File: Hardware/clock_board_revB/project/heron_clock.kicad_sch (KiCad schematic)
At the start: 110 parts, among them J1 5V_IN, J10 PPS_B200_2, J2 PPS_IN, J3 REF_B210_1, J4 REF_B210_2, J5 REF_B200_1, J6 REF_B200_2, J7 PPS_B210_1, J8 PPS_B210_2, J9 PPS_B200_1, U1 TPS7A2033DBVR, U2 TPS7A2033DBVR, U3 SiT5155AI-FK-33E0-10.000000, U4 LMK1C1104PWR, U5 SN74LVC1G17DBVR, U6 SN74LVC125APWR

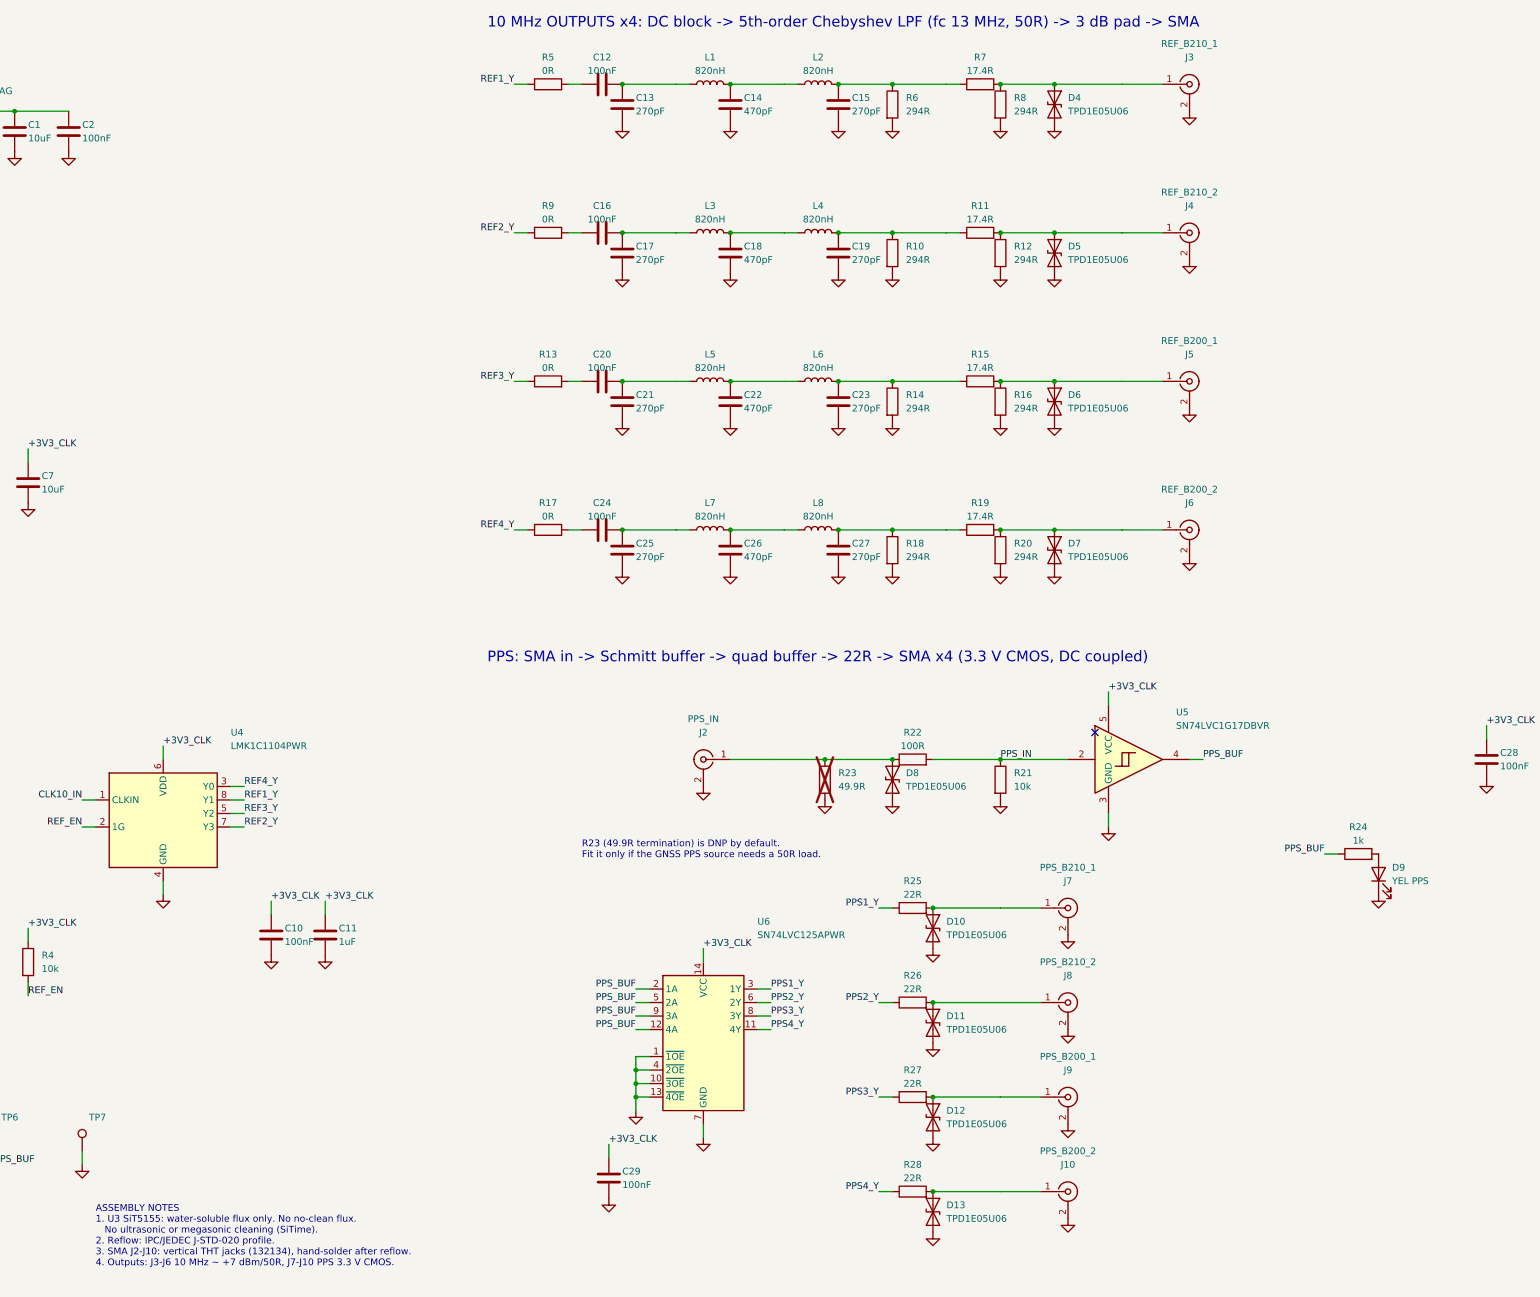
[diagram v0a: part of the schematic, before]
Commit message: Change clock board rev B SDR jacks to SMP blind-mate (D-027)
Change J3-J10 from vertical SMA jacks to Amphenol RF SMP-MSLD-PCT
limited-detent jacks. J2 (PPS IN) stays SMA. The new footprint has
oversize holes (+/-0.20 mm float), so each jack is soldered in place
with its SDR mated. Lead sizes come from the Amphenol IGES model.

Swap the footprints in the existing PCB and keep all routes. Refill
the pours. Move the board title 0.5 mm clear of the larger pads.
Set the R23 DNP flag to match the schematic. Save in KiCad 10 format.
DRC: 0 errors, 0 unconnected pads, 0 parity issues.

Add an export-only mode to make_fab.sh, and let it run on Windows.
Record D-027 and the open values (Q-015) in docs/DECISIONS.md.

Co-Authored-By: Claude Opus 5.5 <noreply@anthropic.com>
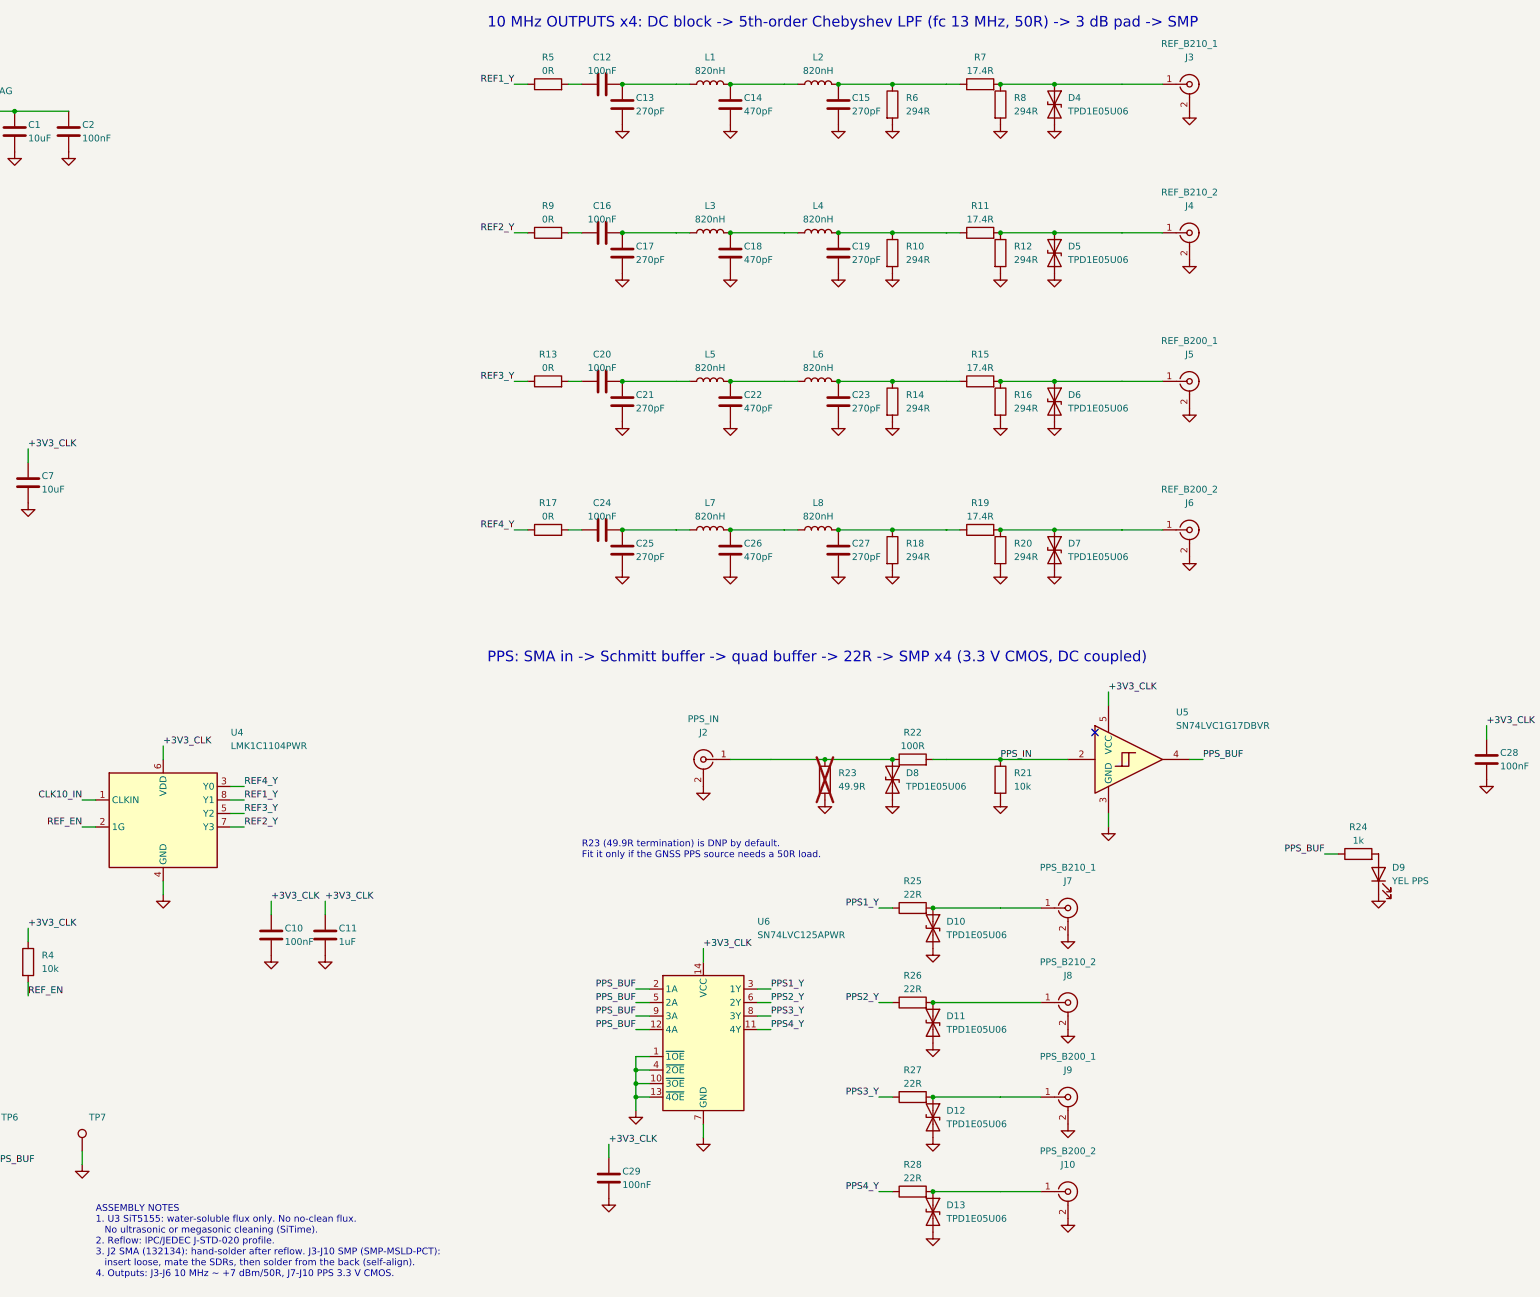
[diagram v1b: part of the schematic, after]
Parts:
- J10, J3, J4, J5, J6, J7, J8, J9: footprint Connector_Coaxial:SMA_Amphenol_132134_Vertical -> HERON_Clock:SMP_Amphenol_SMP-MSLD-PCT_Vertical_Float; MPN 132134 -> SMP-MSLD-PCT
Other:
- note added: "10 MHz OUTPUTS x4: DC block -> 5th-order Chebyshev LPF (fc 13 MHz, 50R) -> 3 dB pad -> SMP"
- note added: "ASSEMBLY NOTES 1. U3 SiT5155: water-soluble flux only. No no-clean flux. No ultrasonic or megasonic cleaning (SiTime). 2. Reflow: IPC/JEDEC J-STD-020 profile. 3. J2 SMA (132134): hand-solder after reflow. J3-J10 SMP (SMP-MSLD-PCT): insert loose, mate the SDRs, then solder from the back (self-align). 4. Outputs: J3-J6 10 MHz ~ +7 dBm/50R, J7-J10 PPS 3.3 V CMOS."
- note added: "PPS: SMA in -> Schmitt buffer -> quad buffer -> 22R -> SMP x4 (3.3 V CMOS, DC coupled)"
- note removed: "10 MHz OUTPUTS x4: DC block -> 5th-order Chebyshev LPF (fc 13 MHz, 50R) -> 3 dB pad -> SMA"
- note removed: "ASSEMBLY NOTES 1. U3 SiT5155: water-soluble flux only. No no-clean flux. No ultrasonic or megasonic cleaning (SiTime). 2. Reflow: IPC/JEDEC J-STD-020 profile. 3. SMA J2-J10: vertical THT jacks (132134), hand-solder after reflow. 4. Outputs: J3-J6 10 MHz ~ +7 dBm/50R, J7-J10 PPS 3.3 V CMOS."
- note removed: "PPS: SMA in -> Schmitt buffer -> quad buffer -> 22R -> SMA x4 (3.3 V CMOS, DC coupled)"
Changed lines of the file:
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@@
           (reference "#PWR020")
           (unit 1)))))
-  (text "10 MHz OUTPUTS x4: DC block -> 5th-order Chebyshev LPF (fc 13 MHz, 50R) -> 3 dB pad -> SMA"
+  (text "10 MHz OUTPUTS x4: DC block -> 5th-order Chebyshev LPF (fc 13 MHz, 50R) -> 3 dB pad -> SMP"
     (at 200.66 22.86 0)
     (effects
@@
         (font
           (size 1.27 1.27))))
-    (property "Footprint" "Connector_Coaxial:SMA_Amphenol_132134_Vertical"
+    (property "Footprint" "HERON_Clock:SMP_Amphenol_SMP-MSLD-PCT_Vertical_Float"
       (at 332.74 35.56 0)
       (effects
@@
         (font
           (size 1.27 1.27)) hide))
-    (property "MPN" "132134"
+    (property "MPN" "SMP-MSLD-PCT"
       (at 332.74 35.56 0)
       (effects
@@
         (font
           (size 1.27 1.27))))
-    (property "Footprint" "Connector_Coaxial:SMA_Amphenol_132134_Vertical"
+    (property "Footprint" "HERON_Clock:SMP_Amphenol_SMP-MSLD-PCT_Vertical_Float"
       (at 332.74 63.5 0)
       (effects
@@
         (font
           (size 1.27 1.27)) hide))
-    (property "MPN" "132134"
+    (property "MPN" "SMP-MSLD-PCT"
       (at 332.74 63.5 0)
       (effects
@@
         (font
           (size 1.27 1.27))))
-    (property "Footprint" "Connector_Coaxial:SMA_Amphenol_132134_Vertical"
+    (property "Footprint" "HERON_Clock:SMP_Amphenol_SMP-MSLD-PCT_Vertical_Float"
       (at 332.74 91.44 0)
       (effects
@@
         (font
           (size 1.27 1.27)) hide))
-    (property "MPN" "132134"
+    (property "MPN" "SMP-MSLD-PCT"
       (at 332.74 91.44 0)
       (effects
@@
         (font
           (size 1.27 1.27))))
-    (property "Footprint" "Connector_Coaxial:SMA_Amphenol_132134_Vertical"
+    (property "Footprint" "HERON_Clock:SMP_Amphenol_SMP-MSLD-PCT_Vertical_Float"
       (at 332.74 119.38 0)
       (effects
@@
         (font
           (size 1.27 1.27)) hide))
-    (property "MPN" "132134"
+    (property "MPN" "SMP-MSLD-PCT"
       (at 332.74 119.38 0)
       (effects
@@
           (reference "#PWR048")
           (unit 1)))))
-  (text "PPS: SMA in -> Schmitt buffer -> quad buffer -> 22R -> SMA x4 (3.3 V CMOS, DC coupled)"
+  (text "PPS: SMA in -> Schmitt buffer -> quad buffer -> 22R -> SMP x4 (3.3 V CMOS, DC coupled)"
     (at 200.66 142.24 0)
     (effects
@@
         (font
           (size 1.27 1.27))))
-    (property "Footprint" "Connector_Coaxial:SMA_Amphenol_132134_Vertical"
+    (property "Footprint" "HERON_Clock:SMP_Amphenol_SMP-MSLD-PCT_Vertical_Float"
       (at 309.88 190.5 0)
       (effects
@@
         (font
           (size 1.27 1.27)) hide))
-    (property "MPN" "132134"
+    (property "MPN" "SMP-MSLD-PCT"
       (at 309.88 190.5 0)
       (effects
@@
         (font
           (size 1.27 1.27))))
-    (property "Footprint" "Connector_Coaxial:SMA_Amphenol_132134_Vertical"
+    (property "Footprint" "HERON_Clock:SMP_Amphenol_SMP-MSLD-PCT_Vertical_Float"
       (at 309.88 208.28 0)
       (effects
@@
         (font
           (size 1.27 1.27)) hide))
-    (property "MPN" "132134"
+    (property "MPN" "SMP-MSLD-PCT"
       (at 309.88 208.28 0)
       (effects
@@
         (font
           (size 1.27 1.27))))
-    (property "Footprint" "Connector_Coaxial:SMA_Amphenol_132134_Vertical"
+    (property "Footprint" "HERON_Clock:SMP_Amphenol_SMP-MSLD-PCT_Vertical_Float"
       (at 309.88 226.06 0)
       (effects
@@
         (font
           (size 1.27 1.27)) hide))
-    (property "MPN" "132134"
+    (property "MPN" "SMP-MSLD-PCT"
       (at 309.88 226.06 0)
       (effects
@@
         (font
           (size 1.27 1.27))))
-    (property "Footprint" "Connector_Coaxial:SMA_Amphenol_132134_Vertical"
+    (property "Footprint" "HERON_Clock:SMP_Amphenol_SMP-MSLD-PCT_Vertical_Float"
       (at 309.88 243.84 0)
       (effects
@@
         (font
           (size 1.27 1.27)) hide))
-    (property "MPN" "132134"
+    (property "MPN" "SMP-MSLD-PCT"
       (at 309.88 243.84 0)
       (effects
@@
           (reference "FID3")
           (unit 1)))))
-  (text "ASSEMBLY NOTES\n1. U3 SiT5155: water-soluble flux only. No no-clean flux.\n   No ultrasonic or megasonic cleaning (SiTime).\n2. Reflow: IPC/JEDEC J-STD-020 profile.\n3. SMA J2-J10: vertical THT jacks (132134), hand-solder after reflow.\n4. Outputs: J3-J6 10 MHz ~ +7 dBm/50R, J7-J10 PPS 3.3 V CMOS."
+  (text "ASSEMBLY NOTES\n1. U3 SiT5155: water-soluble flux only. No no-clean flux.\n   No ultrasonic or megasonic cleaning (SiTime).\n2. Reflow: IPC/JEDEC J-STD-020 profile.\n3. J2 SMA (132134): hand-solder after reflow. J3-J10 SMP (SMP-MSLD-PCT):\n   insert loose, mate the SDRs, then solder from the back (self-align).\n4. Outputs: J3-J6 10 MHz ~ +7 dBm/50R, J7-J10 PPS 3.3 V CMOS."
     (at 127 246.38 0)
     (effects

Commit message: Update clock board rev B BOM, jacks and LDOs for direct SMP mate (D-027)
Change J3-J10 to Amphenol SMP-MSSB-PCT (smooth bore). Take the
footprint dimensions from the Amphenol outline drawing rev B.
Each SDR now uses one Cinch 134-1019-451 SMA-to-SMP adapter. There
is no bullet.

Bring the BOM up to date. Give every resistor an MPN and a tolerance.
Replace parts that are obsolete or have no stock: the 1 uF, 2.2 uF,
10 uF and 100 nF capacitors and D2. Replace U1 with LP5907MFX-3.3 and
U2 with TLV75533PDBVR, because TPS7A2033PDBVR has no stock (same
pinout). Add bom_sources.csv for stock, price, notes and the
off-board adapters. make_bom.py fails when a fitted part has no MPN.

Regenerate the schematic from design.py and sync the PCB fields.
Restore the SMP assembly note. DRC: 0 errors, 0 parity issues.

Co-Authored-By: Claude Opus 5.5 <noreply@anthropic.com>
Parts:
- C1, C7, C9: MPN GRM21BR61C106KE15L -> CC0805KRX5R7BB106; Manufacturer Murata -> YAGEO
- C10, C12, C16, C2, C20, C24, C28, C29, C8: MPN GRM155R71C104KA88D -> CC0402KRX7R7BB104; Manufacturer Murata -> YAGEO
- C11, C3, C5: MPN GRM188R61C105KA93D -> GRM188R61C105KA12D
- C4, C6: MPN GRM188R61A225KE34D -> GRM188R6YA225KA12D
- D2: value PMEG3020EJ -> SS1030HEWS; MPN PMEG3020EJ,115 -> SS1030HEWS_R1_00001; Manufacturer Nexperia -> Panjit
- J10, J3, J4, J5, J6, J7, J8, J9: footprint HERON_Clock:SMP_Amphenol_SMP-MSLD-PCT_Vertical_Float -> HERON_Clock:SMP_Amphenol_SMP-MSSB-PCT_Vertical_Float; MPN SMP-MSLD-PCT -> SMP-MSSB-PCT
- R1, R24: MPN (none) -> RC0402FR-071KL; Manufacturer (none) -> YAGEO; Tolerance (none) -> 1%
- R10, R12, R14, R16, R18, R20, R6, R8: MPN (none) -> ERJ-2RKF2940X; Manufacturer (none) -> Panasonic
- R11, R15, R19, R7: MPN (none) -> RC0402FR-0717R4L; Manufacturer (none) -> YAGEO
- R13, R17, R5, R9: MPN (none) -> RC0402JR-070RL; Manufacturer (none) -> YAGEO; Tolerance 1% -> jumper
- R2, R21, R4: MPN (none) -> RC0402FR-0710KL; Manufacturer (none) -> YAGEO
- R22: MPN (none) -> RC0402FR-07100RL; Manufacturer (none) -> YAGEO; Tolerance (none) -> 1%
- R23: MPN (none) -> RC0402FR-0749R9L; Manufacturer (none) -> YAGEO
- R25, R26, R27, R28: MPN (none) -> RC0402FR-0722RL; Manufacturer (none) -> YAGEO
- R3: MPN (none) -> RC0402FR-0722RL; Manufacturer (none) -> YAGEO; Tolerance (none) -> 1%
- U1: value TPS7A2033DBVR -> LP5907MFX-3.3/NOPB; MPN TPS7A2033DBVR -> LP5907MFX-3.3/NOPB
- U2: value TPS7A2033DBVR -> TLV75533PDBVR; MPN TPS7A2033DBVR -> TLV75533PDBVR
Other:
- note added: "ASSEMBLY NOTES 1. U3 SiT5155: water-soluble flux only. No no-clean flux. No ultrasonic or megasonic cleaning (SiTime). 2. Reflow: IPC/JEDEC J-STD-020 profile. 3. J2 SMA (132134): hand-solder after reflow. J3-J10 SMP (SMP-MSSB-PCT): insert loose, mate the SDRs, then solder from the back (self-align). 4. Outputs: J3-J6 10 MHz ~ +7 dBm/50R, J7-J10 PPS 3.3 V CMOS."
- note removed: "ASSEMBLY NOTES 1. U3 SiT5155: water-soluble flux only. No no-clean flux. No ultrasonic or megasonic cleaning (SiTime). 2. Reflow: IPC/JEDEC J-STD-020 profile. 3. J2 SMA (132134): hand-solder after reflow. J3-J10 SMP (SMP-MSLD-PCT): insert loose, mate the SDRs, then solder from the back (self-align). 4. Outputs: J3-J6 10 MHz ~ +7 dBm/50R, J7-J10 PPS 3.3 V CMOS."
